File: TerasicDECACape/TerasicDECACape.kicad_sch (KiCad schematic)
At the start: 23 parts, among them CN1 NASB0-S6701-TS50, CN2 NASB0-S6701-TS50, J1 MiSTer SDRAM Module, J2 USB_A, J3 Conn_01x03_Male, P8 BeagleBone_Black_Header, P9 BeagleBone_Black_Header, SW1 TS-1187A-B-A-B, SW2 TS-1187A-B-A-B

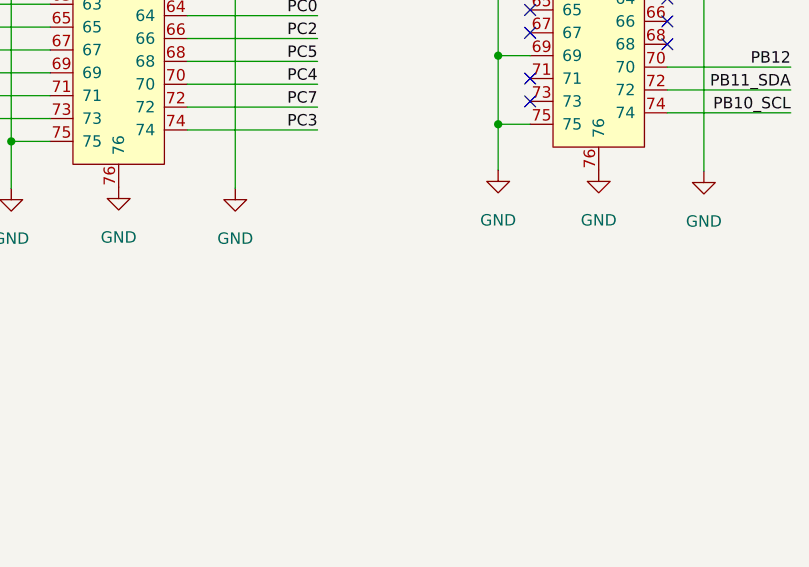
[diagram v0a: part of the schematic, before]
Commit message: add mounting hole for module
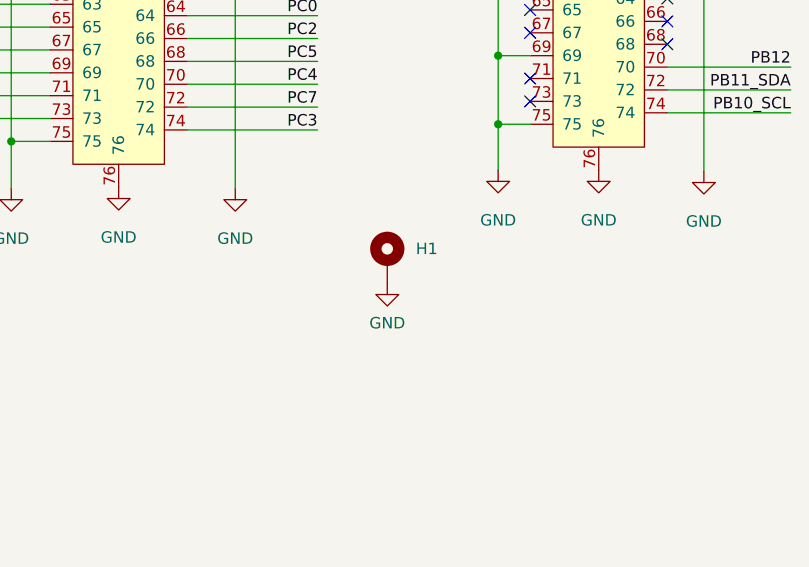
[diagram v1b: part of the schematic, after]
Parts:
- added H1: MountingHole_Pad, MountingHole:MountingHole_2.2mm_M2_ISO7380_Pad_TopBottom, symbol Mechanical:MountingHole_Pad
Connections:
- net GND: now also H1.1
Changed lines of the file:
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@@
     (pin "9")
+  )
+  (symbol (lib_id "Mechanical:MountingHole_Pad") (at 219.075 155.575 0) (unit 1)
+    (in_bom yes) (on_board yes) (fields_autoplaced)
+    (property "Reference" "H1" (id 0) (at 222.25 154.3049 0)
+      (effects (font (size 1.27 1.27)) (justify left))
+    )
+    (property "Value" "MountingHole_Pad" (id 1) (at 222.25 155.5749 0)
+      (effects (font (size 1.27 1.27)) (justify left) hide)
+    )
+    (property "Footprint" "MountingHole:MountingHole_2.2mm_M2_ISO7380_Pad_TopBottom" (id 2) (at 219.075 155.575 0)
+      (effects (font (size 1.27 1.27)) hide)
+    )
+    (property "Datasheet" "~" (id 3) (at 219.075 155.575 0)
+      (effects (font (size 1.27 1.27)) hide)
+    )
+    (pin "1")
   )
   (symbol (lib_id "Connector:Conn_01x03_Male") (at 135.636 58.42 0) (unit 1)
@@
     )
     (property "Datasheet" "" (id 3) (at 87.4268 191.5414 0)
+      (effects (font (size 1.27 1.27)) hide)
+    )
+    (pin "1")
+  )
+  (symbol (lib_id "power:GND") (at 219.075 158.115 0) (unit 1)
+    (in_bom yes) (on_board yes) (fields_autoplaced)
+    (property "Reference" "#PWR0123" (id 0) (at 219.075 164.465 0)
+      (effects (font (size 1.27 1.27)) hide)
+    )
+    (property "Value" "GND" (id 1) (at 219.075 162.56 0))
+    (property "Footprint" "" (id 2) (at 219.075 158.115 0)
+      (effects (font (size 1.27 1.27)) hide)
+    )
+    (property "Datasheet" "" (id 3) (at 219.075 158.115 0)
       (effects (font (size 1.27 1.27)) hide)
     )
@@
       (reference "#PWR0122") (unit 1) (value "+3V3") (footprint "")
     )
+    (path "/9d836500-d5a1-4807-8474-cc10742ddfce"
+      (reference "#PWR0123") (unit 1) (value "GND") (footprint "")
+    )
     (path "/351874dc-99f1-41fb-8357-28151f7d437e"
       (reference "C1") (unit 1) (value "100nF") (footprint "C_0402_1005Metric")
@@
       (reference "F1") (unit 1) (value "JK-NSMD050-30V") (footprint "easyeda2kicad:F1206")
     )
+    (path "/206d5ec0-ce8e-4ca6-969b-c3bad25858b8"
+      (reference "H1") (unit 1) (value "MountingHole_Pad") (footprint "MountingHole:MountingHole_2.2mm_M2_ISO7380_Pad_TopBottom")
+    )
     (path "/8ea390cf-7fda-4a12-9fac-1aa7bec354c3"

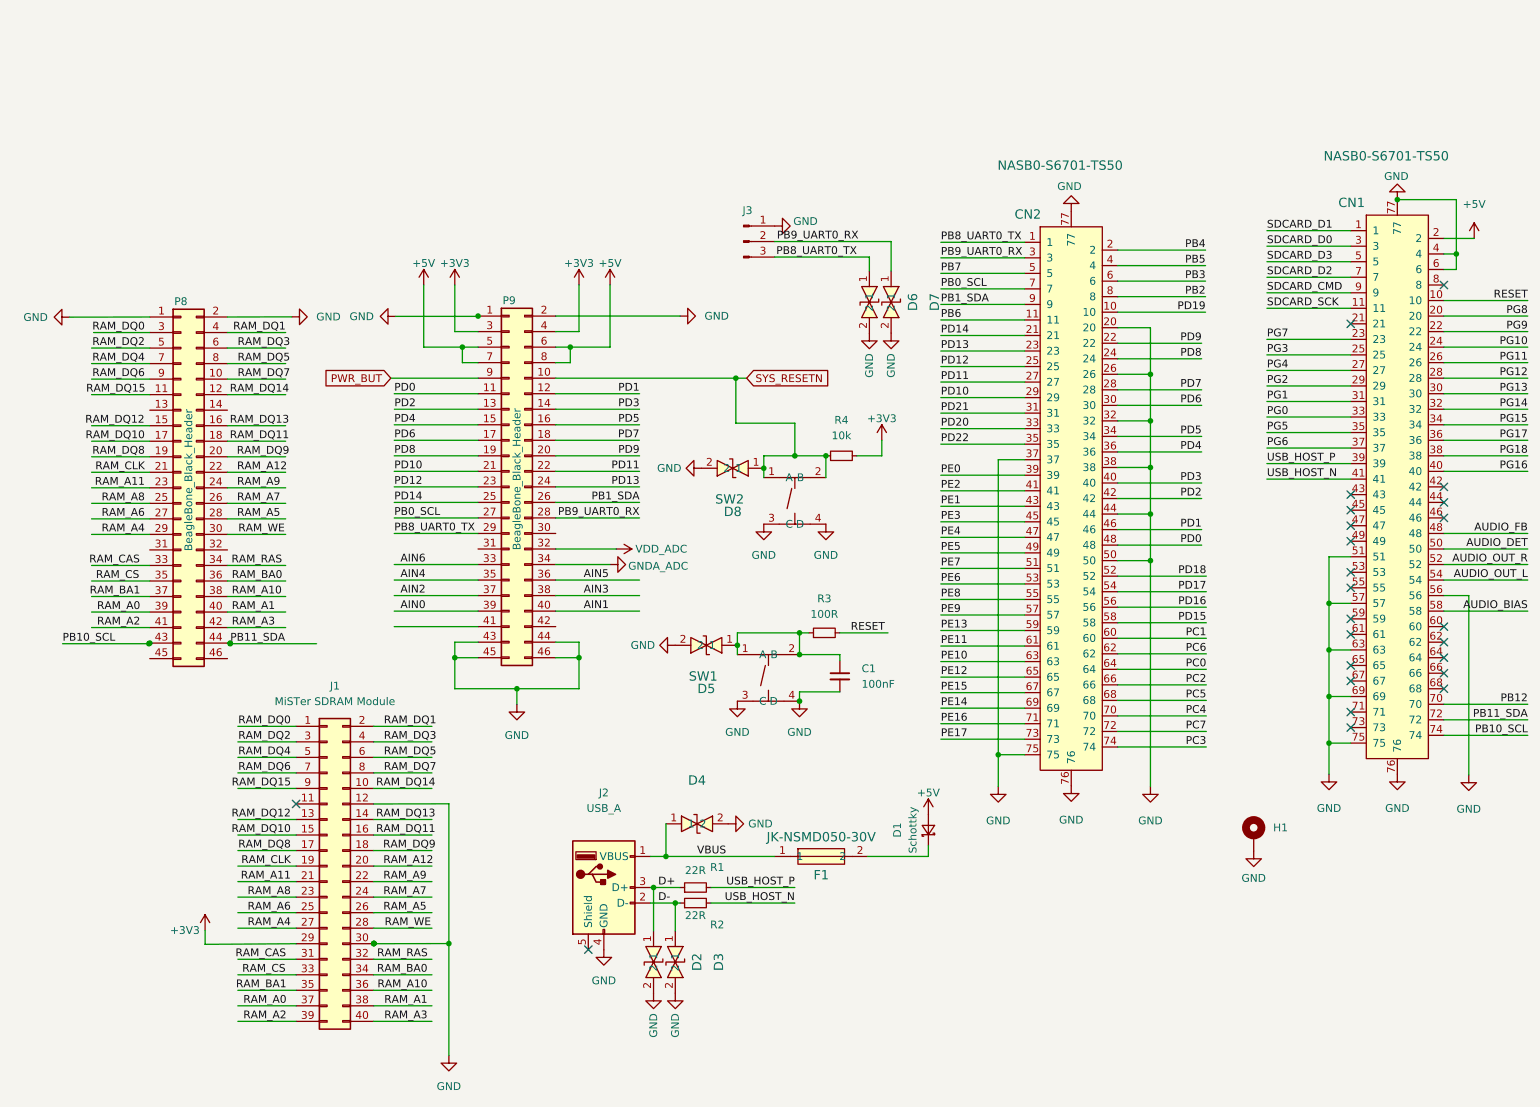
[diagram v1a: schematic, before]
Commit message: add user IO header, connect UART1 with flow control
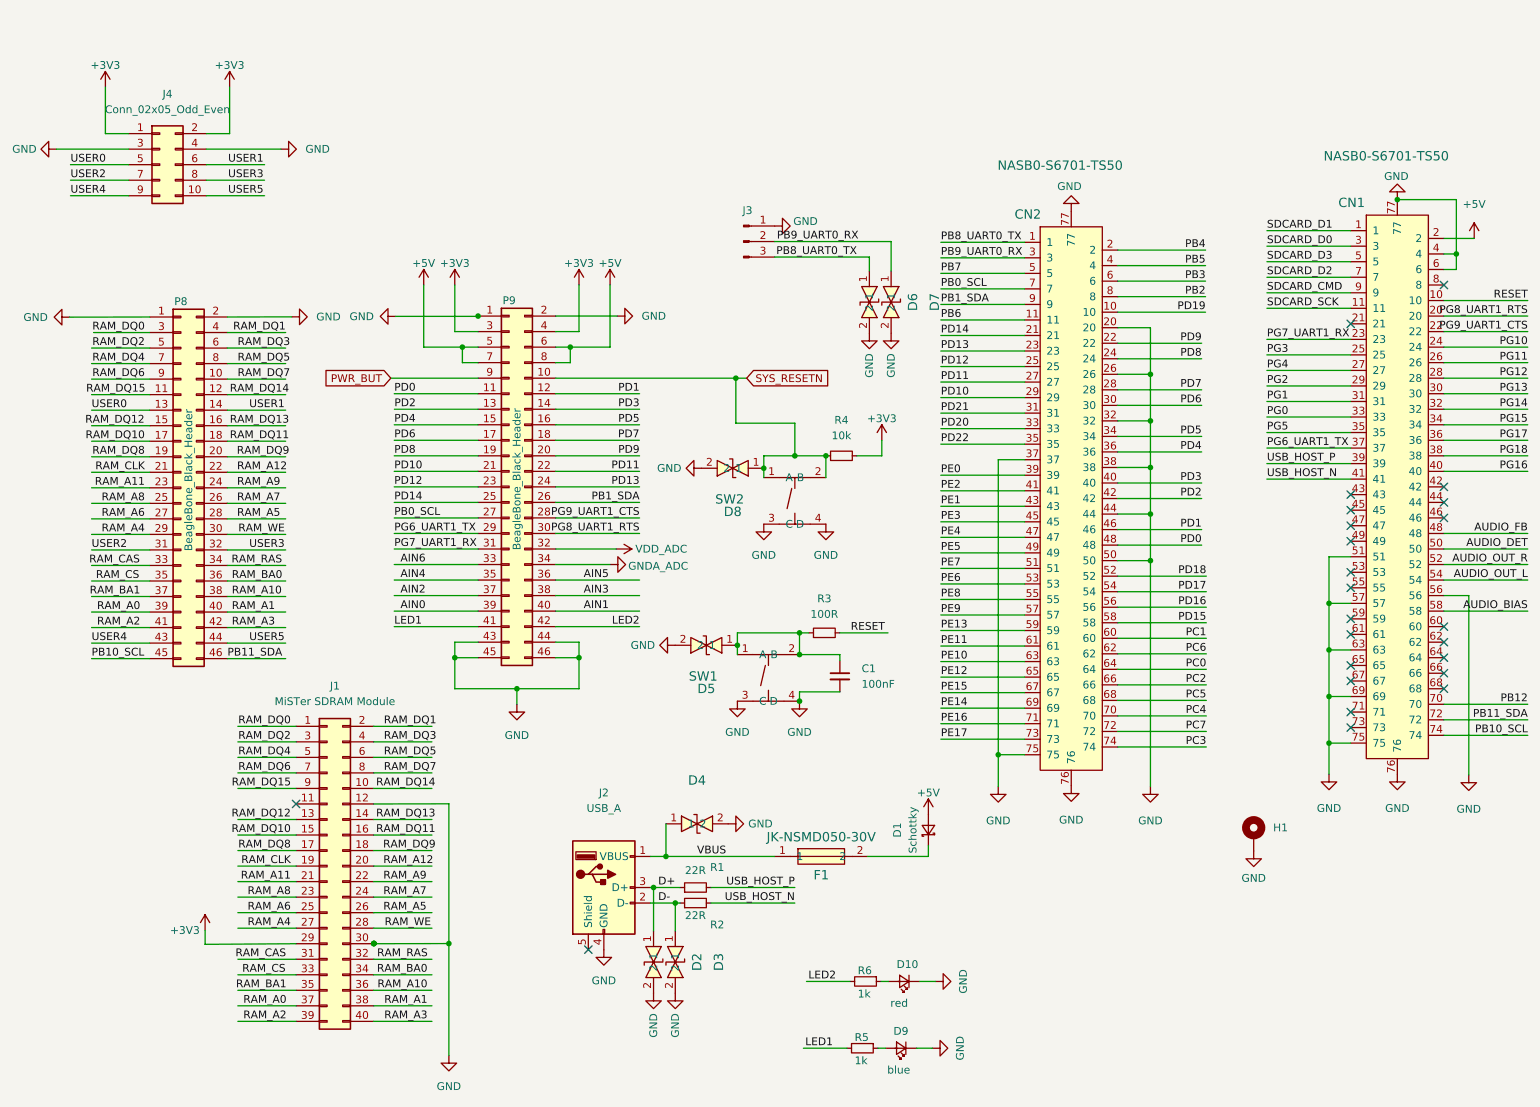
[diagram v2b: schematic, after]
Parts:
- added D10: red, LED_SMD:LED_0603_1608Metric, symbol Device:LED_Small
- added D9: blue, LED_SMD:LED_0603_1608Metric, symbol Device:LED_Small
- added J4: Conn_02x05_Odd_Even, Connector_PinSocket_2.54mm:PinSocket_2x05_P2.54mm_Vertical, symbol Connector_Generic:Conn_02x05_Odd_Even
- added R5, R6: 1k, Resistor_SMD:R_0603_1608Metric, symbol Device:R_Small
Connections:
- net PG7 is gone; now on net PG7_UART1_RX: CN1.23
- net PG8 is gone; now on net PG8_UART1_RTS: CN1.20
- net +3V3: now also J4.1 (Pin_1), J4.2 (Pin_2)
- net GND: now also D10.1 (K), D9.1 (K), J4.3 (Pin_3), J4.4 (Pin_4)
- net PB10_SCL: now also P8.45 (Pin_45); no longer P8.43 (Pin_43)
- net PB11_SDA: now also P8.46 (Pin_46); no longer P8.44 (Pin_44)
- net PB8_UART0_TX: no longer P9.29 (Pin_29)
- net PB9_UART0_RX: no longer P9.28 (Pin_28)
- net PG8_UART1_RTS: now reaches P9.30 (Pin_30)
- net PG7_UART1_RX: now reaches P9.31 (Pin_31)
- net LED1: now reaches P9.41 (Pin_41)
- net LED1: now also R5.2
- net LED2: now reaches P9.42 (Pin_42)
- net LED2: now also R6.2
- net USER0: now reaches P8.13 (Pin_13)
- net USER0: now also J4.5 (Pin_5)
- net USER1: now reaches P8.14 (Pin_14)
- net USER1: now also J4.6 (Pin_6)
- net USER2: now reaches P8.31 (Pin_31)
- net USER2: now also J4.7 (Pin_7)
- net USER3: now reaches P8.32 (Pin_32)
- net USER3: now also J4.8 (Pin_8)
- net PG6 renamed PG6_UART1_TX
- net PG6_UART1_TX: now also P9.29 (Pin_29)
- net PG9 renamed PG9_UART1_CTS
- net PG9_UART1_CTS: now also P9.28 (Pin_28)
- new net: D10.2 (A), R6.1
- new net: D9.2 (A), R5.1
- new net USER4: J4.9 (Pin_9), P8.43 (Pin_43)
- new net USER5: J4.10 (Pin_10), P8.44 (Pin_44)

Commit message: add title block data
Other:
- company: (none) -> Hans Baier
- title: (none) -> MiSTeX Allwinner D1 cape for Terasic DECA
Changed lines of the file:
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@@
 (kicad_sch (version 20211123) (generator eeschema)
   (paper "A4")
+  (title_block
+    (title "MiSTeX Allwinner D1 cape for Terasic DECA")
+    (date "2023-03-02")
+    (rev "rev0")
+    (company "Hans Baier")
+  )
   (junction (at 231.394 125.222) (diameter 0) (color 0 0 0 0)
   )

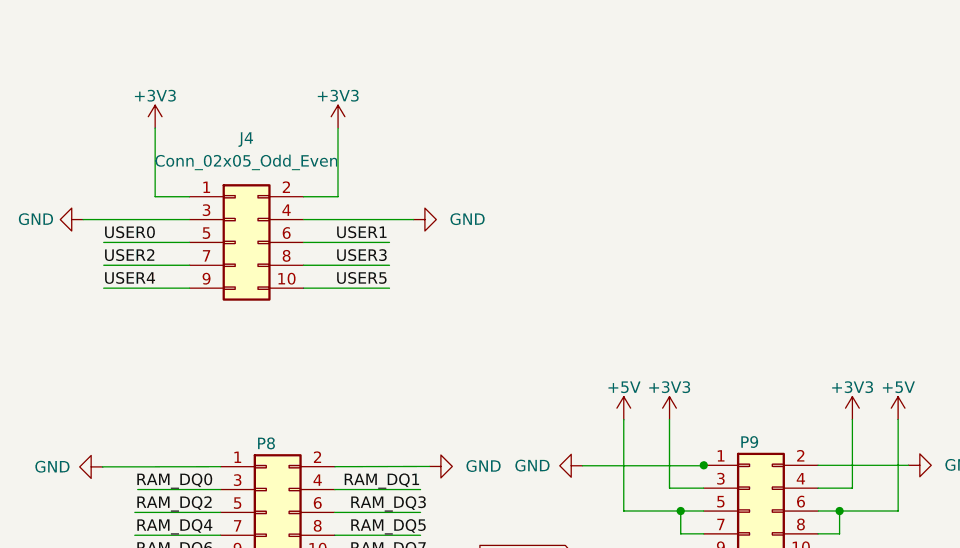
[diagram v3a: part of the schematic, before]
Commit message: fix DRC issues
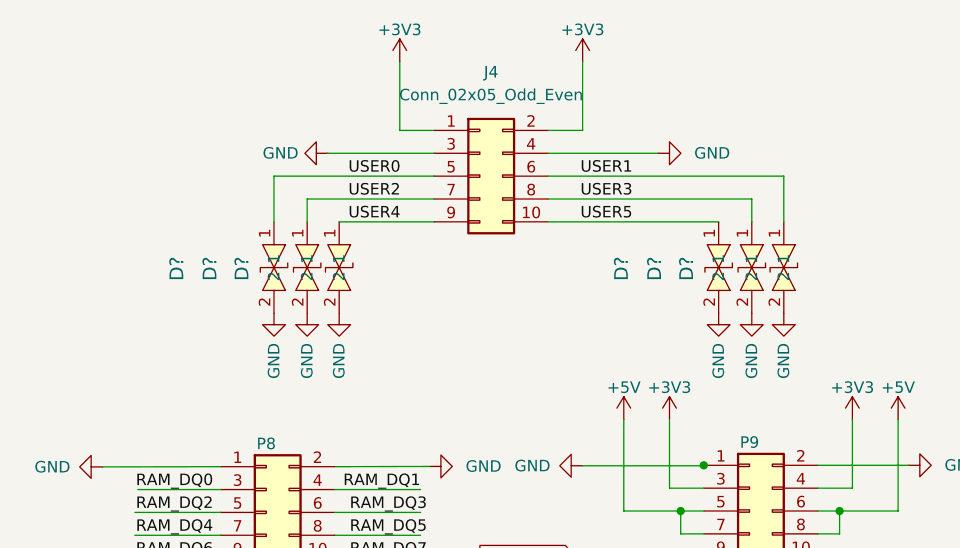
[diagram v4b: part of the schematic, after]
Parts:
- added D? (x6): LXES15AAA1-133, D0402-BI, symbol easyeda2kicad:LXES15AAA1-133
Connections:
- net GND: now also D?.2, D?.2, D?.2, D?.2, D?.2, D?.2
- net USER0: now also D?.1
- net USER1: now also D?.1
- net USER2: now also D?.1
- net USER3: now also D?.1
- net USER4: now also D?.1
- net USER5: now also D?.1
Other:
- moved on the sheet: J4
